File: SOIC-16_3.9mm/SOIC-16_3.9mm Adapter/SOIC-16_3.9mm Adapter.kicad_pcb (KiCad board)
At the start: 2 copper layers, 19.1 x 22.9 mm, 3 parts, among them J1 Conn_01x08, J2 Conn_01x08, U1 16-Pin_Chip

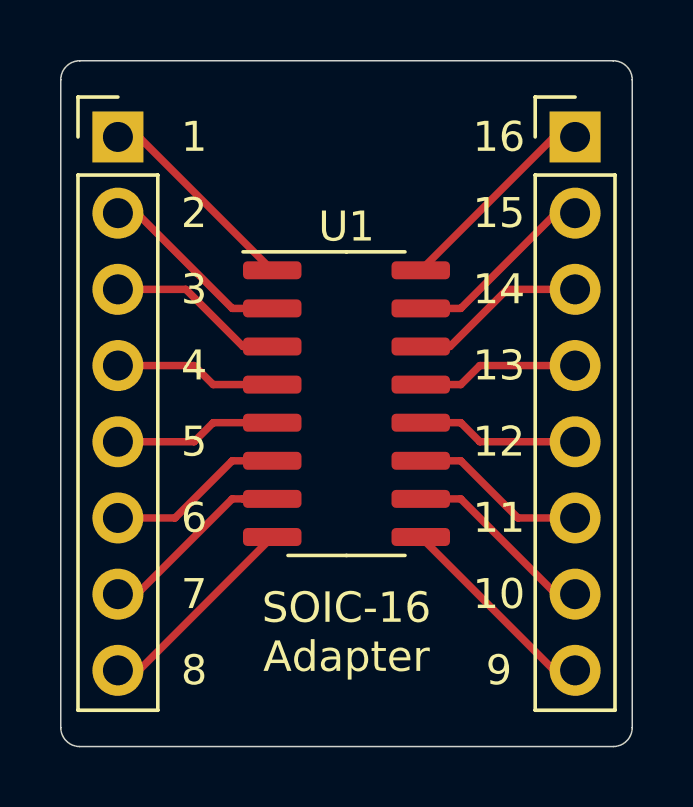
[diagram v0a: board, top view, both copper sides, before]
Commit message: SOICW board added
Some old files deleted... and library changed
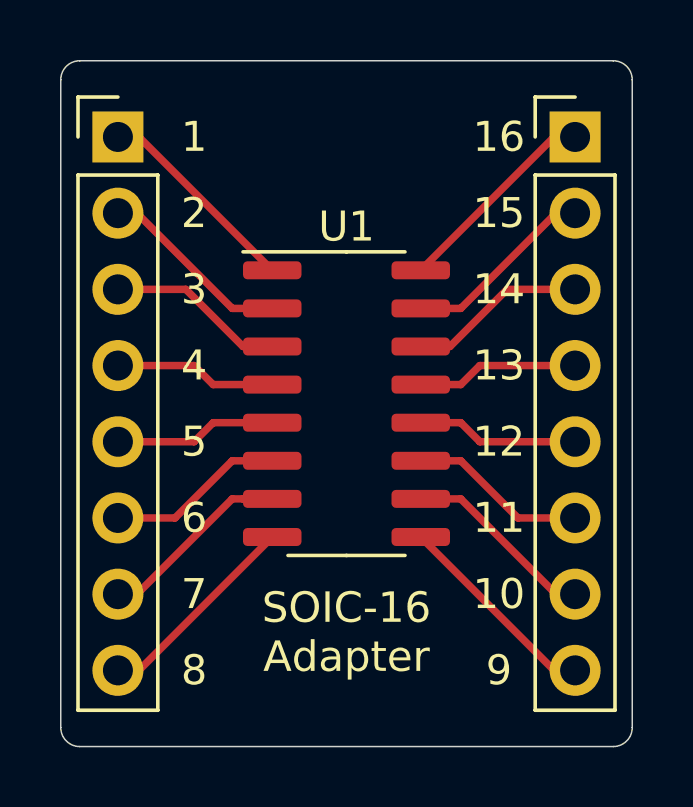
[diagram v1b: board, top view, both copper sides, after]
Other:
- outline, holes or cut-outs redrawn
- net class Default removed
